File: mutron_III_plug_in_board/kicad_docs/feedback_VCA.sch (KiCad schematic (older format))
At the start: 16 parts, among them Q1 BCM847, Q2 MMBT3904, U3 TL072

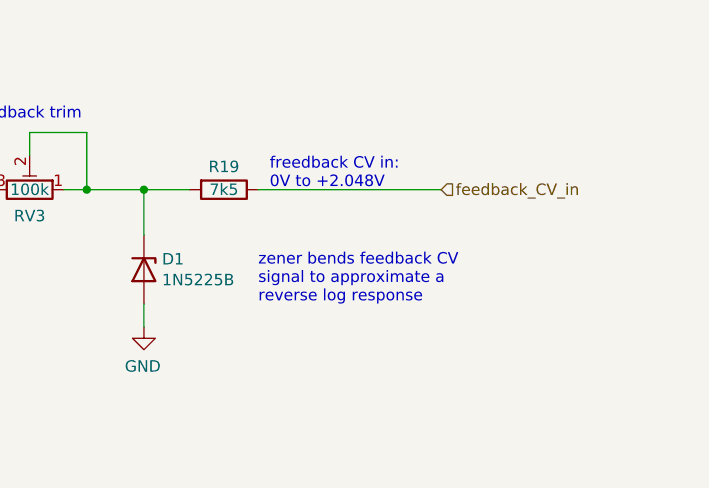
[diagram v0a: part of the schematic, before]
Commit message: change zener
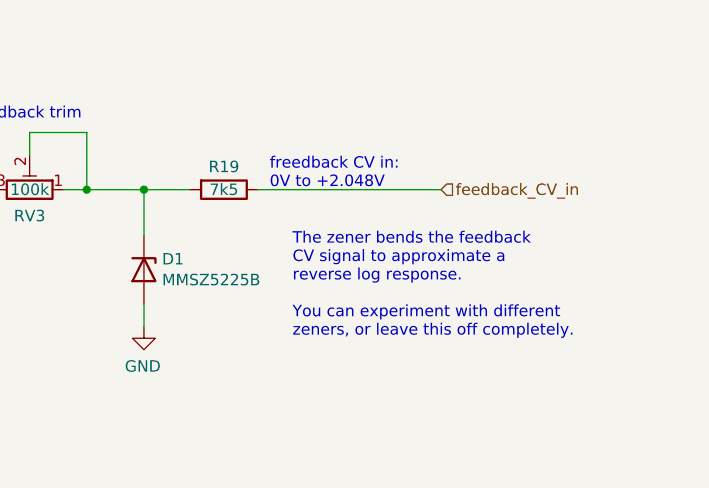
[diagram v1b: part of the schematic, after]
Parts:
- D1: value 1N5225B -> MMSZ5225B
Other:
- note added: "The zener bends the feedback\nCV signal to approximate a \nreverse log response.\n\nYou can experiment with different \nzeners, or leave this off completely."
- note removed: "zener bends feedback CV\nsignal to approximate a \nreverse log response"
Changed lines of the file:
@@
 Text Notes 6850 4350 0    50   ~ 0
 feedback trim
-Text Notes 8100 5150 0    50   ~ 0
-zener bends feedback CV\nsignal to approximate a \nreverse log response
+Text Notes 8250 5300 0    50   ~ 0
+The zener bends the feedback\nCV signal to approximate a \nreverse log response.\n\nYou can experiment with different \nzeners, or leave this off completely.
 Wire Wire Line
 	7600 5250 7600 5150
@@
 AR Path="/5F2781EF/5F2FFAC0" Ref="D1"  Part="1"
 F 0 "D1" V 7554 5079 50  0000 L CNN
-F 1 "1N5225B" V 7645 5079 50  0000 L CNN
+F 1 "MMSZ5225B" V 7645 5079 50  0000 L CNN
 F 2 "Diode_SMD:D_SOD-123" H 7600 5000 50  0001 C CNN
 F 3 "~" H 7600 5000 50  0001 C CNN
